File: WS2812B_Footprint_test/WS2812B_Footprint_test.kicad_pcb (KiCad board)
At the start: 2 copper layers, 13 x 10 mm, 4 parts, among them P1 CONN_01X04

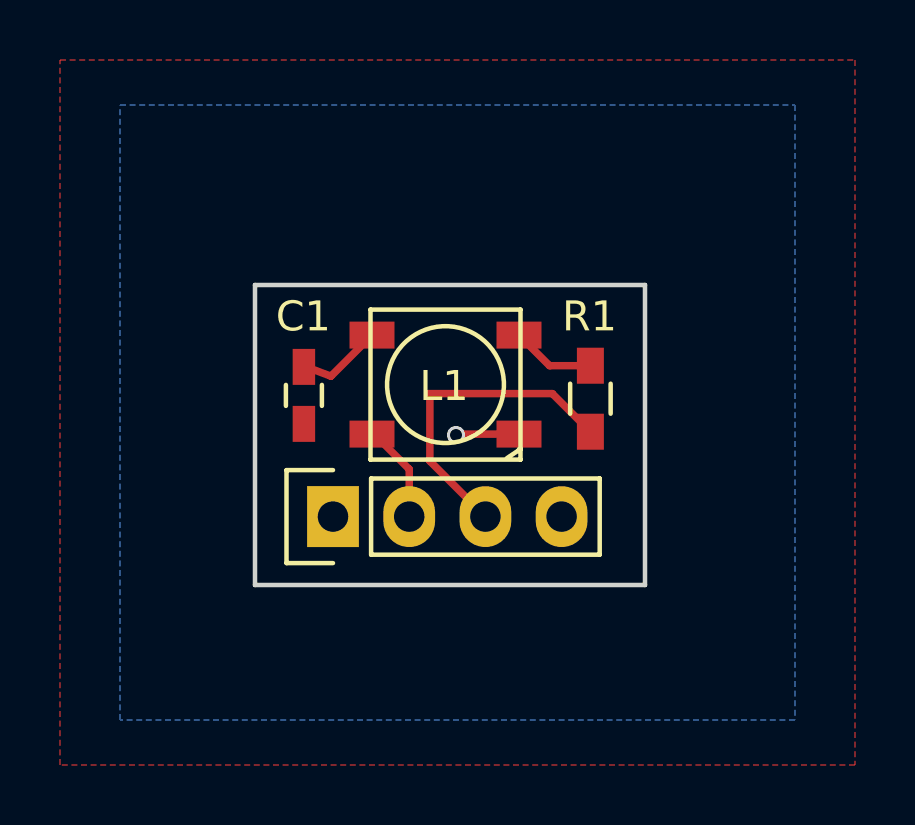
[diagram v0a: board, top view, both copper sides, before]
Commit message: WS2812B Footprint test changes
After getting back the boards from OSHPark, I noticed a design flaw
related to the capacitor and the VCC of the LED chip.  I corrected the
flaw, re-plotted the Gerber files and sent them to OSHPark for fab.
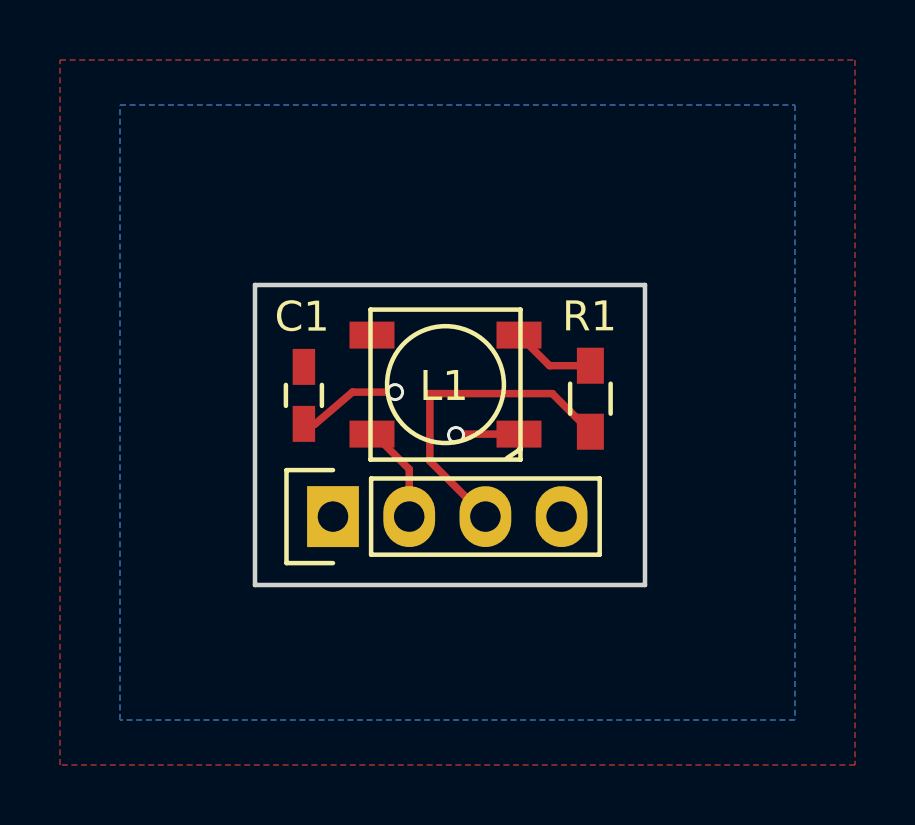
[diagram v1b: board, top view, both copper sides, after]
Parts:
- turned C1 to 270 degrees
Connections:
- C1 pad 2: Net-(C1-Pad2) -> GND
- L1 pad 1: Net-(C1-Pad2) -> PWR
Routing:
- net GND: track 2.11 -> 5.54 mm, vias 1 -> 2
- net Net-(C1-Pad2): track 2.76 -> 0.00 mm
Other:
- board text added: "160204"
- board text added: "WS2812B r1B"
- board text removed: "160115"
- board text removed: "WS2812B r1A"
